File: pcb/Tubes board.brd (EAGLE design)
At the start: 39 x 48.2 mm, 5 parts, among them J2 MAIN POWER, J3 LED DAT, J4 LED POWER, M1 WIRELESS-NRF24L01

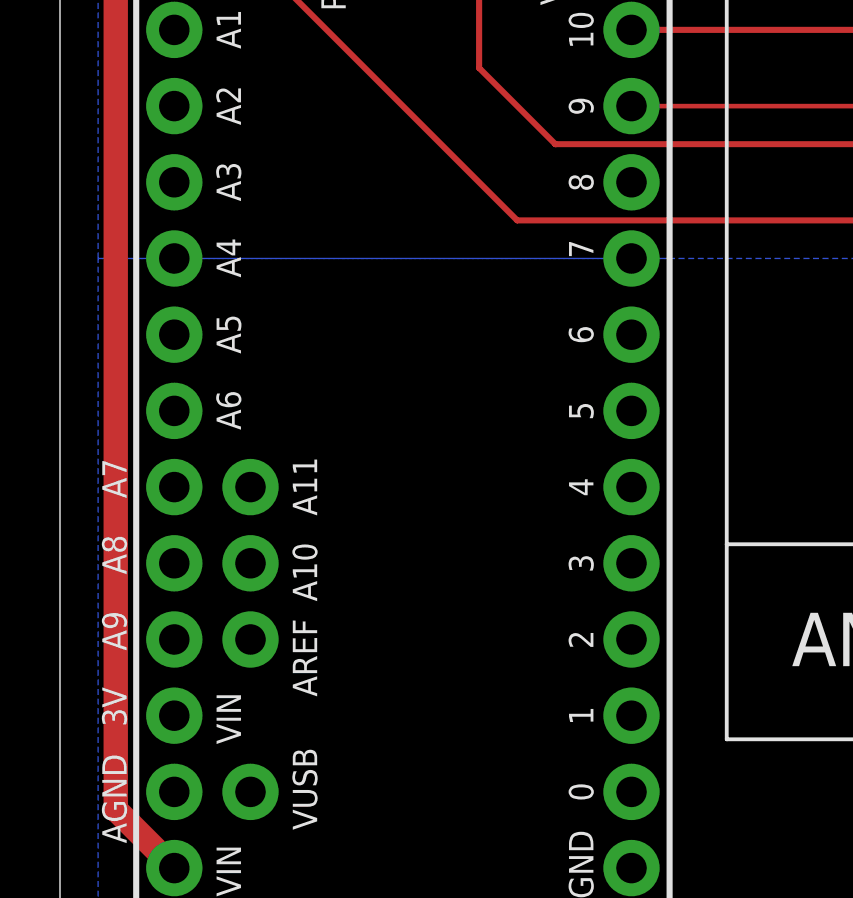
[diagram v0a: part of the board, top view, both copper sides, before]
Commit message: Add missing wire
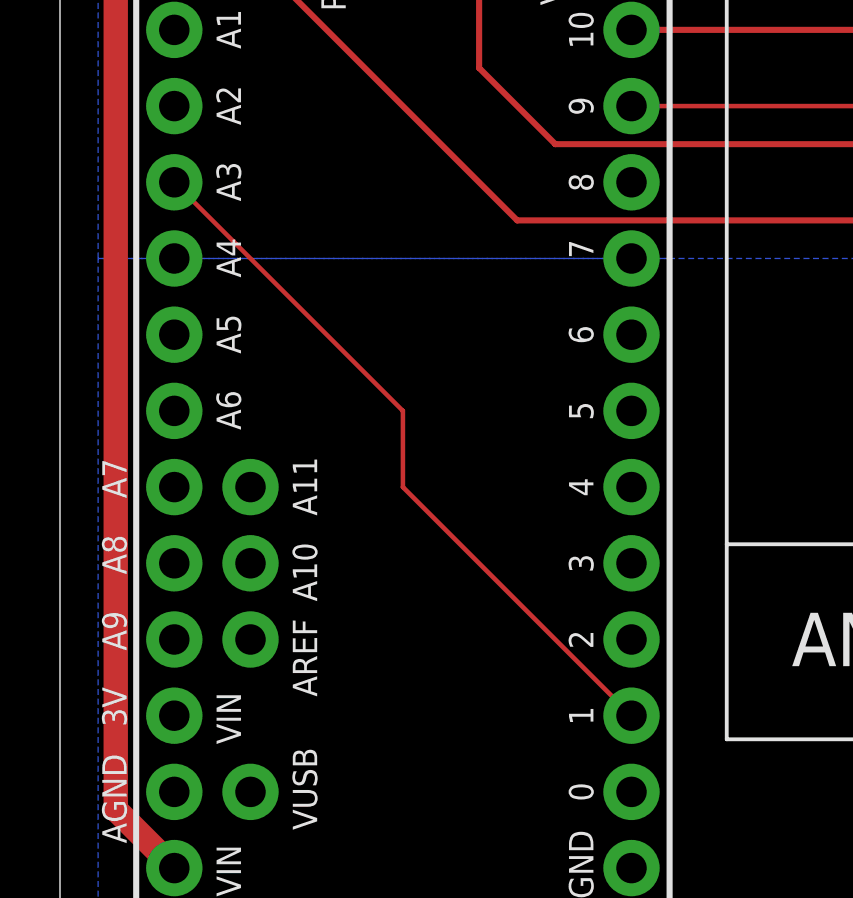
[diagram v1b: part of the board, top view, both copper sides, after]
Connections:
- new net N$1: B1.VBAT, J3.1
- net DAT: now also B1.1, B1.17; no longer B1.VBAT, J3.1
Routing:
- net N$1: track 0.00 -> 22.4 mm
- net DAT: track 22.4 -> 24.1 mm
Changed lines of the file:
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@@
 </signal>
 <signal name="DAT">
-<contactref element="J3" pad="1"/>
-<contactref element="B1" pad="VBAT"/>
-<wire x1="17.78" y1="54.61" x2="17.78" y2="57.15" width="0.2032" layer="1"/>
-<wire x1="17.78" y1="57.15" x2="20.32" y2="59.69" width="0.2032" layer="1"/>
-<wire x1="20.32" y1="59.69" x2="33.02" y2="59.69" width="0.2032" layer="1"/>
-<wire x1="33.02" y1="59.69" x2="35.56" y2="62.23" width="0.2032" layer="1"/>
+<contactref element="B1" pad="1"/>
+<contactref element="B1" pad="17"/>
+<wire x1="20.32" y1="26.67" x2="12.7" y2="34.29" width="0.1524" layer="1"/>
+<wire x1="12.7" y1="34.29" x2="12.7" y2="36.83" width="0.1524" layer="1"/>
+<wire x1="12.7" y1="36.83" x2="5.08" y2="44.45" width="0.1524" layer="1"/>
 </signal>
 <signal name="VUSB">
@@
 <wire x1="34.417" y1="53.213" x2="34.29" y2="53.213" width="0.1524" layer="1"/>
 </signal>
+<signal name="N$1">
+<contactref element="J3" pad="1"/>
+<contactref element="B1" pad="VBAT"/>
+<wire x1="17.78" y1="54.61" x2="17.78" y2="57.15" width="0.2032" layer="1"/>
+<wire x1="17.78" y1="57.15" x2="20.32" y2="59.69" width="0.2032" layer="1"/>
+<wire x1="20.32" y1="59.69" x2="33.02" y2="59.69" width="0.2032" layer="1"/>
+<wire x1="33.02" y1="59.69" x2="35.56" y2="62.23" width="0.2032" layer="1"/>
+</signal>
 </signals>

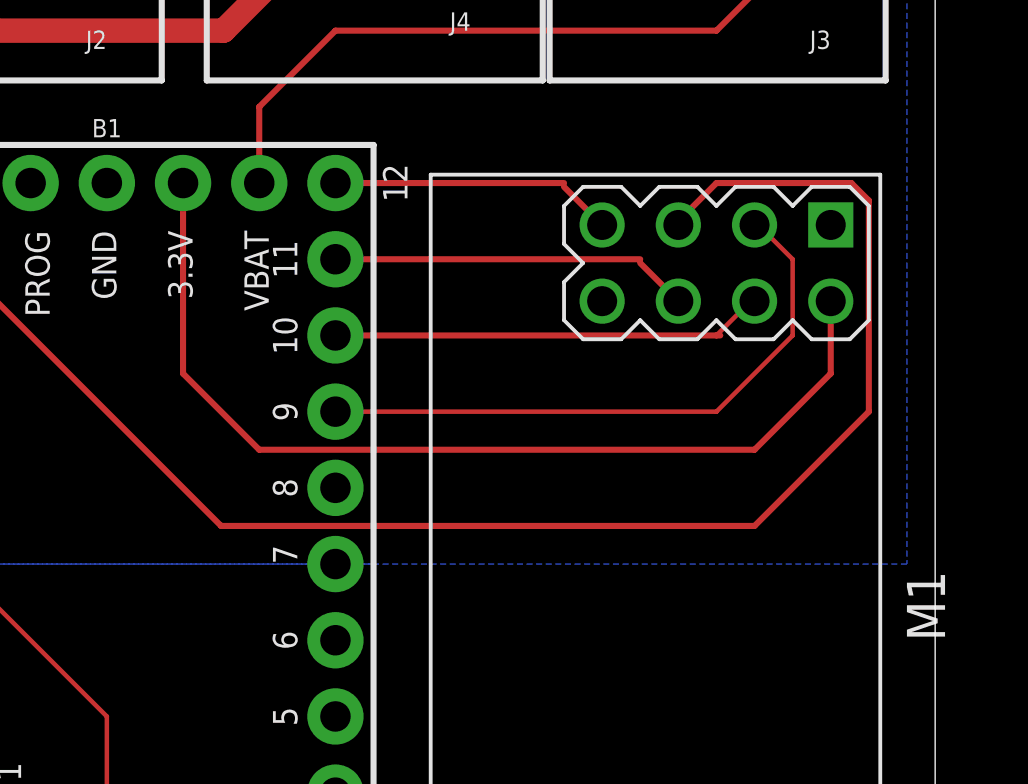
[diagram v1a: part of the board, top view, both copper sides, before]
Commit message: Wire IRQ
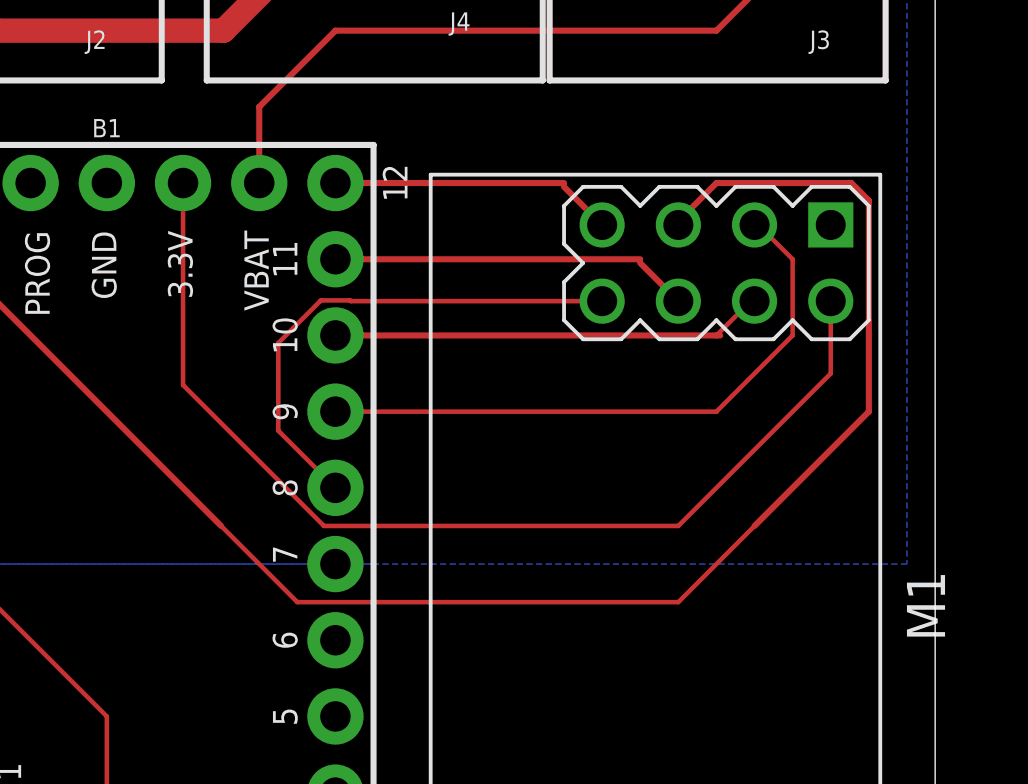
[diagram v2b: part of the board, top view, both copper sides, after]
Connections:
- net N$1 renamed LED_DAT
- new net IRQ: B1.8, M1.8
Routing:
- net IRQ: track 0.00 -> 17.0 mm
- net +3.3V: track 32.5 -> 34.8 mm
- net SCK: track 53.6 -> 55.7 mm
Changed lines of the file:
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@@
 <contactref element="M1" pad="2"/>
 <contactref element="B1" pad="3.3V"/>
-<wire x1="15.24" y1="54.61" x2="15.24" y2="48.26" width="0.2032" layer="1"/>
-<wire x1="15.24" y1="48.26" x2="17.78" y2="45.72" width="0.2032" layer="1"/>
-<wire x1="17.78" y1="45.72" x2="34.29" y2="45.72" width="0.2032" layer="1"/>
-<wire x1="34.29" y1="45.72" x2="36.83" y2="48.26" width="0.2032" layer="1"/>
-<wire x1="36.83" y1="48.26" x2="36.83" y2="50.673" width="0.2032" layer="1"/>
+<wire x1="36.83" y1="50.673" x2="36.83" y2="48.26" width="0.1524" layer="1"/>
+<wire x1="36.83" y1="48.26" x2="31.75" y2="43.18" width="0.1524" layer="1"/>
+<wire x1="19.93763125" y1="43.18" x2="31.75" y2="43.18" width="0.1524" layer="1"/>
+<wire x1="15.24" y1="54.61" x2="15.24" y2="47.87763125" width="0.1524" layer="1"/>
+<wire x1="15.24" y1="47.87763125" x2="19.93763125" y2="43.18" width="0.1524" layer="1"/>
 </signal>
 <signal name="CS">
@@
 <contactref element="B1" pad="13"/>
 <wire x1="5.08" y1="54.61" x2="16.51" y2="43.18" width="0.2032" layer="1"/>
-<wire x1="16.51" y1="43.18" x2="34.29" y2="43.18" width="0.2032" layer="1"/>
-<wire x1="38.1" y1="46.99" x2="34.29" y2="43.18" width="0.2032" layer="1"/>
+<wire x1="34.29" y1="43.18" x2="38.1" y2="46.99" width="0.2032" layer="1"/>
 <wire x1="31.75" y1="53.213" x2="31.75" y2="53.34" width="0.1524" layer="1"/>
 <wire x1="33.02" y1="54.61" x2="31.75" y2="53.34" width="0.2032" layer="1"/>
@@
 <wire x1="37.5182875" y1="54.61" x2="38.1" y2="54.0282875" width="0.2032" layer="1"/>
 <wire x1="33.02" y1="54.61" x2="37.5182875" y2="54.61" width="0.2032" layer="1"/>
+<wire x1="16.51" y1="43.18" x2="19.05" y2="40.64" width="0.1524" layer="1"/>
+<wire x1="19.05" y1="40.64" x2="31.75" y2="40.64" width="0.1524" layer="1"/>
+<wire x1="31.75" y1="40.64" x2="34.29" y2="43.18" width="0.1524" layer="1"/>
 </signal>
 <signal name="MOSI">
@@
 <wire x1="34.417" y1="53.213" x2="34.29" y2="53.213" width="0.1524" layer="1"/>
 </signal>
-<signal name="N$1">
+<signal name="LED_DAT">
 <contactref element="J3" pad="1"/>
 <contactref element="B1" pad="VBAT"/>
@@
 <wire x1="33.02" y1="59.69" x2="35.56" y2="62.23" width="0.2032" layer="1"/>
 </signal>
+<signal name="IRQ">
+<contactref element="M1" pad="8"/>
+<contactref element="B1" pad="8"/>
+<wire x1="29.21" y1="50.673" x2="20.82936875" y2="50.673" width="0.1524" layer="1"/>
+<wire x1="20.82936875" y1="50.673" x2="20.80396875" y2="50.6984" width="0.1524" layer="1"/>
+<wire x1="20.80396875" y1="50.6984" x2="19.83603125" y2="50.6984" width="0.1524" layer="1"/>
+<wire x1="19.83603125" y1="50.6984" x2="19.81063125" y2="50.673" width="0.1524" layer="1"/>
+<wire x1="20.32" y1="44.45" x2="18.415" y2="46.355" width="0.1524" layer="1"/>
+<wire x1="18.415" y1="46.355" x2="18.415" y2="49.27736875" width="0.1524" layer="1"/>
+<wire x1="18.415" y1="49.27736875" x2="19.81063125" y2="50.673" width="0.1524" layer="1"/>
+</signal>
 </signals>
